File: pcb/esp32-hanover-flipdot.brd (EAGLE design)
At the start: 45.1 x 25.4 mm, 28 parts, among them J1 DC-005, J2 HANOVER, J3 FTDI, Q1 NCE3407A, Q2 S9013, U1 ESP32-PICO-D4, U2 CJA1117B-3.3-SOT89, U3 LM2576S

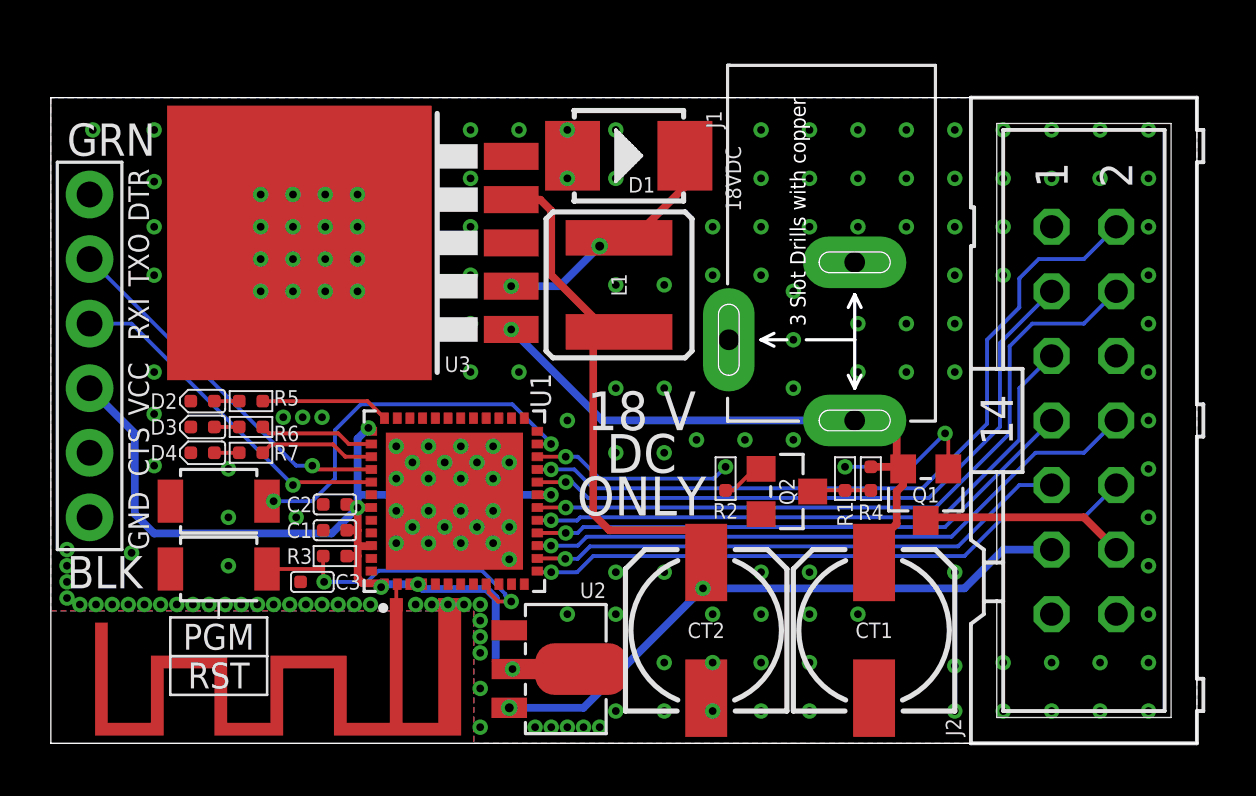
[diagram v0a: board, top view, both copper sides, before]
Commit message: PCB: Layout improvements and parts substitutions
Board:
* Increase ground plane stitching especially for heatsinking of regulators and ESP32
* Add pour and stitching on +3V3 LDO regulator for heatsinking
* Increase voltage trace sizes to conduct heat away from power components/decrease voltage droop

Schematic:
* Disconnect dot board pin 14 from 18V, it seems to cause erratic behavior on dot boards. Not sure what the function of this 18V supply pin is, but boards work fine with this line snipped off
* Add dot board pin 13 to existing COIL_PULSE net on pin 14, as they are internally shorted on the dot boards - this should double the current capacity/halve the voltage droop on the cable to the first dot board
* Parts swapped with latest Eagle online libraries where applicable

Schematic/BoM:
* D2, D3, D4: Swap from blue LEDs to white LEDs
* R5, R6, R7: Swap from 100R to 150R (LED current limiting resistors)
* RST, PGM: Swap to substitute part with same dimensions on Seeed OPL as original part no longer available
* U3: Swap BoM MPN to LM2576SX-5.0/NOPB as it has ready pricing on Seeed Fusion PCBA

Library:
* Add custom library for Seeed 5.5/2.1 DC jack without polarity silkscreen, use it on board

Misc:
* Generate latest Gerbers for Seeed Fusion PCB 2 layer
* Update board image
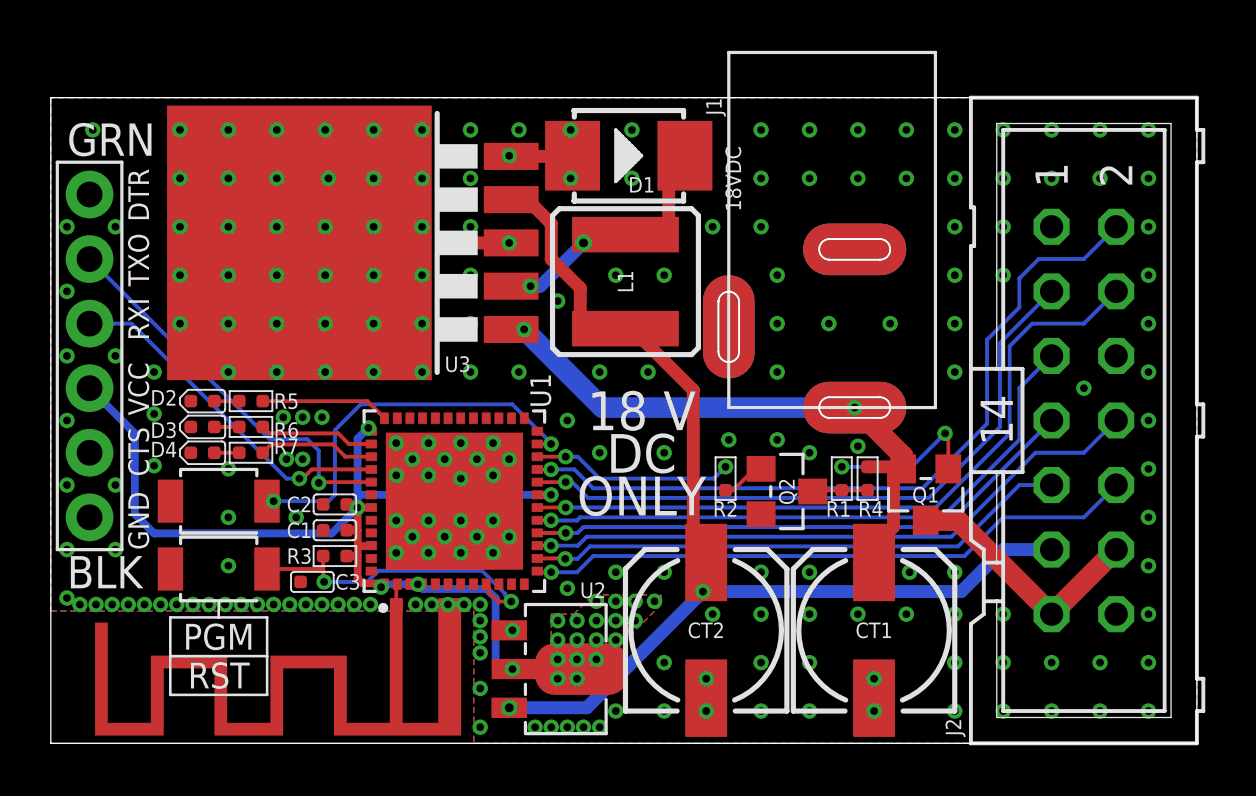
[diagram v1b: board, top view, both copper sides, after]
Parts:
- C1, C2, C3: device Seeed-Capacitor:C0402 -> OPL_Capacitor:C0402
- CT1, CT2: device Seeed-Capacitor:ELECTRO-SMD-C-6MM -> OPL_Capacitor:ELECTRO-SMD-C-6MM
- D1: device Seeed-Diode:DO-214AA -> OPL_Discrete_Semiconductor:DO-214AA
- D2, D3, D4: value BLUE-0402 -> PURE-WHITE-0402; device Seeed-LED:LED-0402 -> OPL_Optoelectronics:LED-0402
- J1: device Seeed-Connector:DCJ3P-14.2X11.0X9.0MM -> OPL_Connector_DC-005_No_Polarity_Markings:3P-L14.2*W11.0*H9.0MM
- PGM, RST: device Seeed-Switch:SW2-2.6-3.0X2.5X1.2+0.4MM -> OPL_Switch:SW2-2.6-3.0X2.5X1.2+0.4MM
- Q1, Q2: device Seeed-Transistor:SOT-23 -> OPL_Discrete_Semiconductor:SOT-23
- R1, R2, R3, R4: device Seeed-Resistor:R0402 -> OPL_Resistor:R0402
- R5, R6, R7: value 100R -> 150R; device Seeed-Resistor:R0402 -> OPL_Resistor:R0402
- U2: device Seeed-IC:SOT-89 -> OPL_IC:SOT-89
- moved J1 0.51 mm to (31.6, 16.4)
- moved L1 0.28 mm to (22.6, 18.2)
- moved R1 0.13 mm to (31.1, 10.4)
- moved R4 0.13 mm to (32.1, 10.4)
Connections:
- net +18V: now also J1.+B, J1.+T; no longer J1.+
- net COIL_PULSE: now also J2.13
- net ESP_RXI: now also J3.P$3; no longer J3.P$2
- net ESP_TXO: now also J3.P$2; no longer J3.P$3
- net GND: now also J1.-1B, J1.-1T, J1.-2B, J1.-2T; no longer J1.-1, J1.-2
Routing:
- net GND: track 0.00 -> 4.40 mm, vias 194 -> 220
- net +5V: track 46.4 -> 44.3 mm
- net COIL_PULSE: track 8.15 -> 10.1 mm
- net ESP_TXO: track 13.8 -> 15.5 mm
- net +18V: track 24.4 -> 23.4 mm, vias 1 -> 2
- net ESP_RXI: track 14.5 -> 13.8 mm
- net N$4: track 9.67 -> 10.2 mm
- net +3V3: vias 6 -> 24
- added copper zone on layer 1, net +3V3
- added copper zone on layer 16, net +3V3

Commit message: PCB: Cleanup for Seeed Fusion
Board and Schematic:
* Change LM2576 part to match BOM

Other documents:
* Exported a new set of Gerbers and matching pick and place files and top of PCB drawing
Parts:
- CT1: value 220UF -> 100UF
- L1: value 3.3µH/±30%/3.4A -> 220uH
- PGM, RST: value B3U-1000P-2P-SMD -> TD-1183SN-A3N-D1R
- U3: value LM2576S -> LM2576SX-5.0/NOPB
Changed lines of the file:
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@@
 <attribute name="VALUE" x="13.589" y="4.191" size="0.6096" layer="27" font="vector" ratio="20" rot="R180" align="top-center"/>
 </element>
-<element name="RST" library="OPL_Switch" library_urn="urn:adsk.eagle:library:8004989" package="SW2-2.6-3.0X2.5X1.2+0.4MM" package3d_urn="urn:adsk.eagle:package:8005100/1" value="B3U-1000P-2P-SMD" x="6.604" y="6.858" smashed="yes">
+<element name="RST" library="OPL_Switch" library_urn="urn:adsk.eagle:library:8004989" package="SW2-2.6-3.0X2.5X1.2+0.4MM" package3d_urn="urn:adsk.eagle:package:8005100/1" value="TD-1183SN-A3N-D1R" x="6.604" y="6.858" smashed="yes">
 <attribute name="MPN" value="B3U-1000P-2P-SMD" x="6.604" y="6.858" size="1.778" layer="27" display="off"/>
 <attribute name="NAME" x="6.604" y="2.667" size="1.016" layer="25" ratio="11" align="center"/>
@@
 <attribute name="VALUE" x="33.655" y="9.144" size="0.889" layer="27" font="vector" ratio="11" rot="R90"/>
 </element>
-<element name="PGM" library="OPL_Switch" library_urn="urn:adsk.eagle:library:8004989" package="SW2-2.6-3.0X2.5X1.2+0.4MM" package3d_urn="urn:adsk.eagle:package:8005100/1" value="B3U-1000P-2P-SMD" x="6.604" y="9.525" smashed="yes">
+<element name="PGM" library="OPL_Switch" library_urn="urn:adsk.eagle:library:8004989" package="SW2-2.6-3.0X2.5X1.2+0.4MM" package3d_urn="urn:adsk.eagle:package:8005100/1" value="TD-1183SN-A3N-D1R" x="6.604" y="9.525" smashed="yes">
 <attribute name="MPN" value="B3U-1000P-2P-SMD" x="6.604" y="9.525" size="1.778" layer="27" display="off"/>
 <attribute name="NAME" x="6.604" y="4.191" size="1.016" layer="25" ratio="11" align="center"/>
 <attribute name="VALUE" x="5.104" y="6.985" size="0.635" layer="27" ratio="11"/>
 </element>
-<element name="U3" library="LM2576 (1)" package="TO263-5" value="LM2576S" x="12.319" y="19.685" smashed="yes" rot="R90">
+<element name="U3" library="LM2576 (1)" package="TO263-5" value="LM2576SX-5.0/NOPB" x="12.319" y="19.685" smashed="yes" rot="R90">
 <attribute name="AVAILABILITY" value="Unavailable" x="12.319" y="19.685" size="1.778" layer="27" rot="R90" display="off"/>
 <attribute name="DESCRIPTION" value=" Integrated Circuit " x="12.319" y="19.685" size="1.778" layer="27" rot="R90" display="off"/>
@@
 <attribute name="VALUE" x="17.9163" y="26.554409375" size="1.272109375" layer="27" rot="R180"/>
 </element>
-<element name="CT1" library="OPL_Capacitor" library_urn="urn:adsk.eagle:library:8004261" package="ELECTRO-SMD-C-6MM" package3d_urn="urn:adsk.eagle:package:8004282/1" value="220UF" x="32.385" y="4.445" smashed="yes" rot="R90">
+<element name="CT1" library="OPL_Capacitor" library_urn="urn:adsk.eagle:library:8004261" package="ELECTRO-SMD-C-6MM" package3d_urn="urn:adsk.eagle:package:8004282/1" value="100UF" x="32.385" y="4.445" smashed="yes" rot="R90">
 <attribute name="MPN" value="302030000" x="32.385" y="4.445" size="1.778" layer="27" rot="R90" display="off"/>
 <attribute name="NAME" x="32.385" y="4.445" size="0.6096" layer="25" ratio="11" align="center"/>
@@
 <element name="D1" library="OPL_Discrete_Semiconductor" library_urn="urn:adsk.eagle:library:8004488" package="DO-214AA" package3d_urn="urn:adsk.eagle:package:8004541/1" value="28V-5A" x="22.733" y="23.114" smashed="yes">
 <attribute name="MPN" value="SS54B" x="22.733" y="23.114" size="1.778" layer="27" display="off"/>
+<attribute name="NAME" x="24.003" y="23.114" size="0.5" layer="33" ratio="10" rot="R180"/>
 <attribute name="NAME" x="23.241" y="21.971" size="0.6096" layer="25" ratio="11" align="center"/>
-<attribute name="NAME" x="24.003" y="23.114" size="0.5" layer="33" ratio="10" rot="R180"/>
 <attribute name="VALUE" x="21.082" y="20.32" size="0.635" layer="27" ratio="10"/>
 </element>
@@
 <attribute name="VALUE" x="30.099" y="1.905" size="0.635" layer="27" ratio="10" rot="R90"/>
 </element>
-<element name="L1" library="SparkFun-Coils" library_urn="urn:adsk.eagle:library:512" package="CR54" package3d_urn="urn:adsk.eagle:package:37572/1" value="3.3µH/±30%/3.4A" x="22.606" y="18.161" smashed="yes">
+<element name="L1" library="SparkFun-Coils" library_urn="urn:adsk.eagle:library:512" package="CR54" package3d_urn="urn:adsk.eagle:package:37572/1" value="220uH" x="22.606" y="18.161" smashed="yes">
 <attribute name="NAME" x="22.606" y="18.161" size="0.6096" layer="25" ratio="11" rot="R270" align="center"/>
 <attribute name="PROD_ID" value="NDUC-11157" x="22.606" y="18.161" size="1.778" layer="27" display="off"/>
